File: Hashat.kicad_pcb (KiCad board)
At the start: 2 copper layers, 65 x 56.5 mm, 101 parts, among them IC1 BM1397_mode1, J1 Raspberry_Pi_2_3, J3 Conn_01x05, J4 Conn_01x04, Q1 CSD17311Q5, Q2 CSD17311Q5, U1 25MHz, U10 DS4432U+, U3 SN74AXC1T45DBVR, U5 MCP1824T-1802E, U6 MCP1824T-0802E, U7 EMC2101, U9 TPS40305

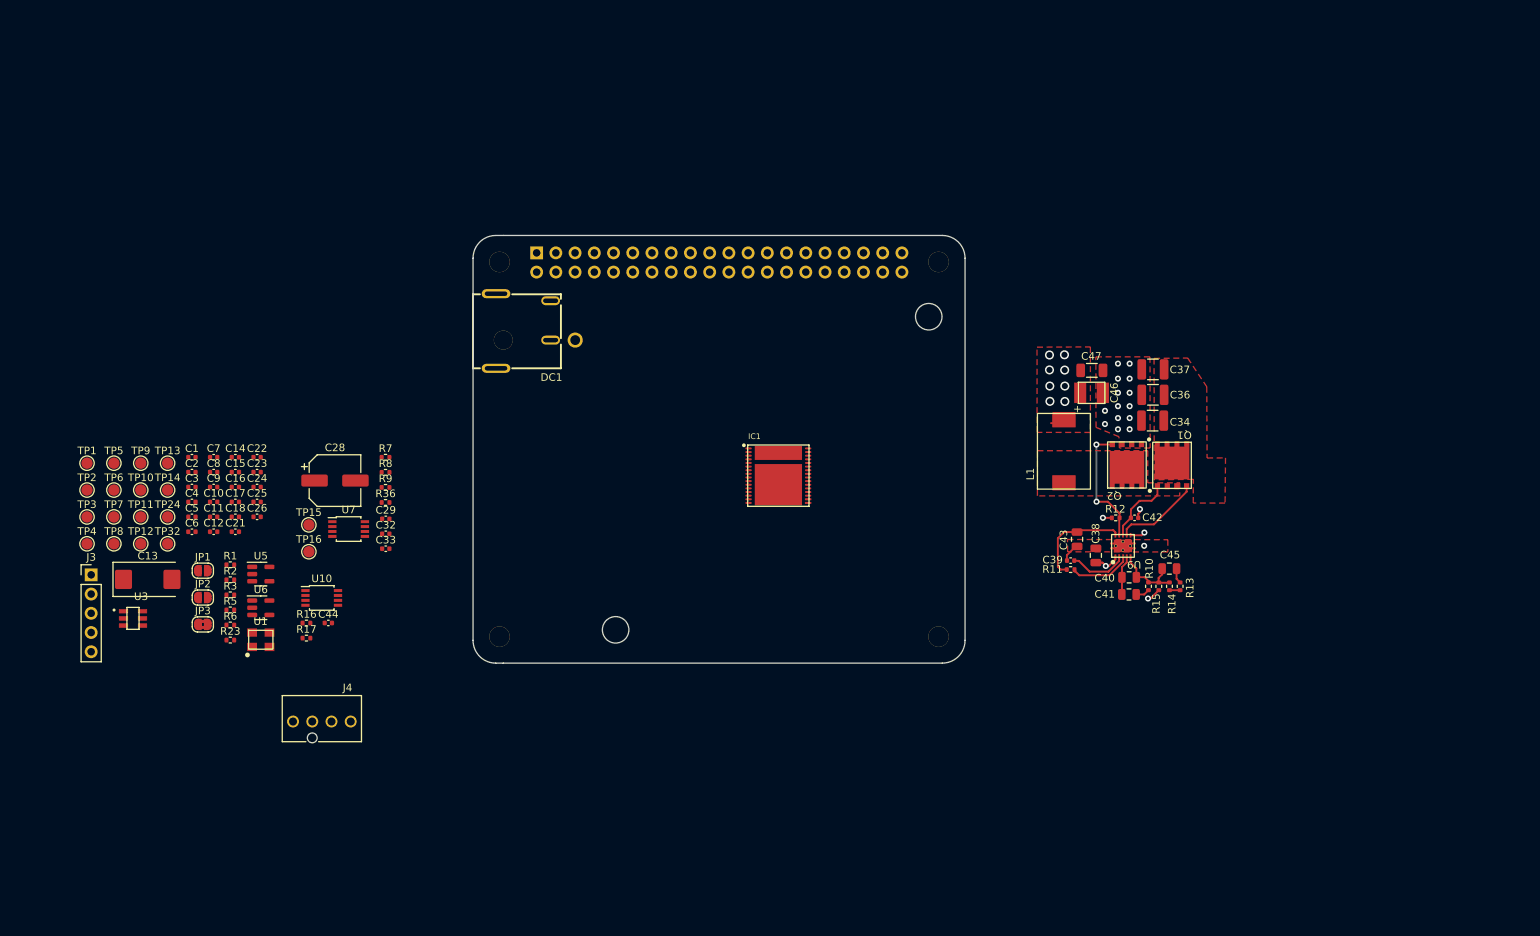
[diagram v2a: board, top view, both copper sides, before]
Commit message: matched up layout ref with schematic
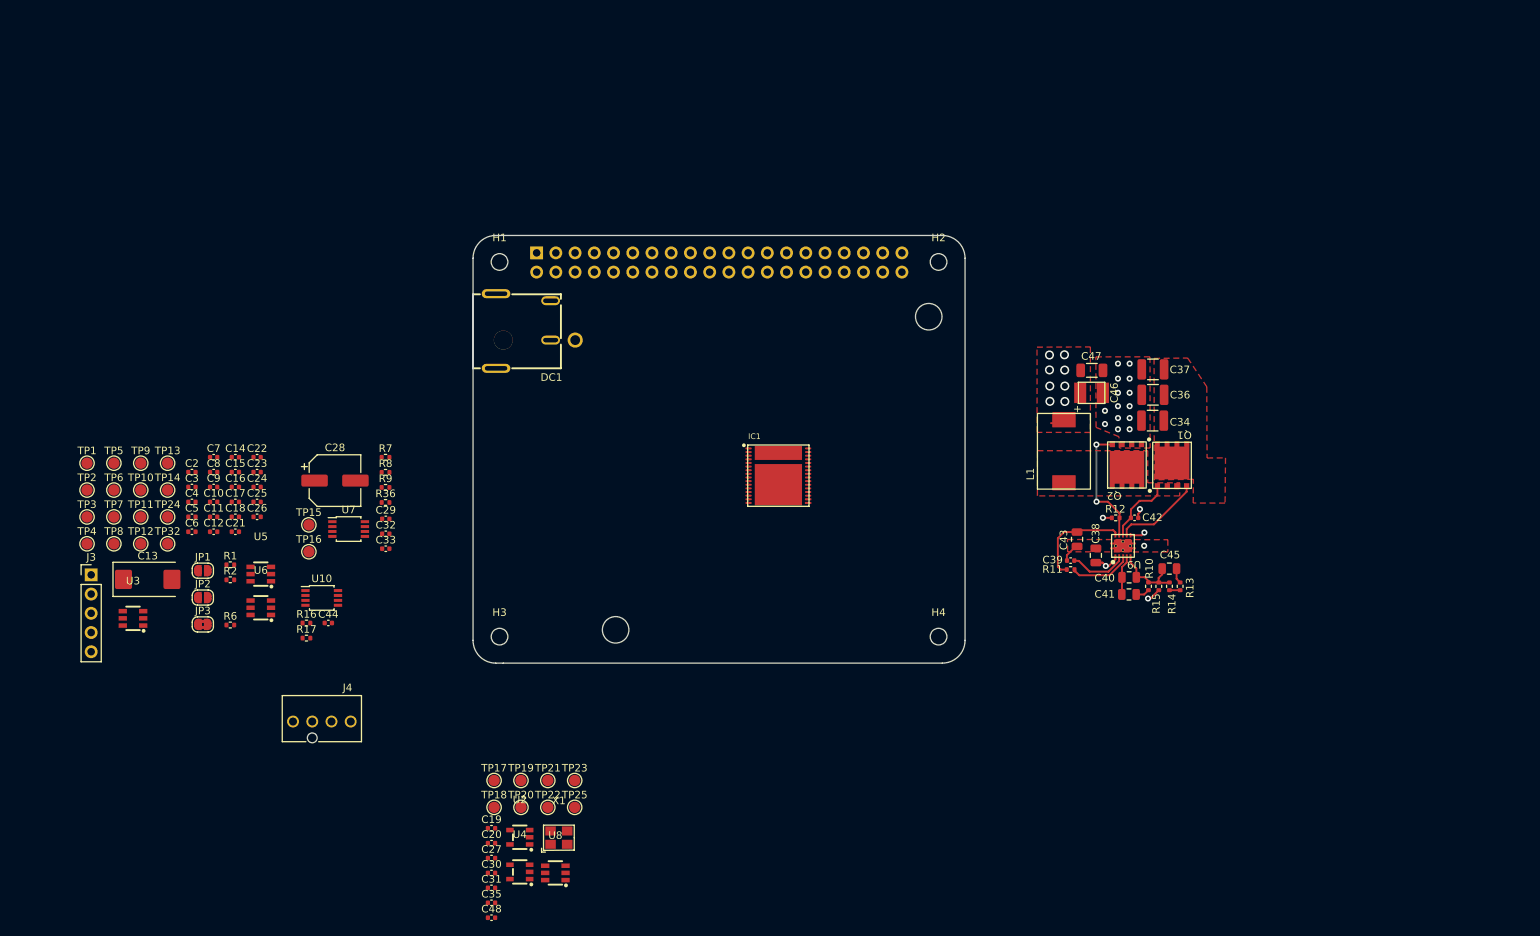
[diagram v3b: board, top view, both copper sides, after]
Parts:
- removed C1: 311-3342-1-ND, Capacitor_SMD:C_0402_1005Metric
- removed R23, R3, R5: 0, Resistor_SMD:R_0402_1005Metric
- removed U1: 25MHz, bitaxe:O 25,0-JO32-B-1V3-1-T1-LF
- added C19: 1uF, Capacitor_SMD:C_0402_1005Metric, F.Cu at (79.4, 133.8)
- added C20: 2.2uF, Capacitor_SMD:C_0402_1005Metric, F.Cu at (79.4, 135.8)
- added C27: 311-3342-1-ND, Capacitor_SMD:C_0402_1005Metric, F.Cu at (79.4, 137.8)
- added C30: 311-3342-1-ND, Capacitor_SMD:C_0402_1005Metric, F.Cu at (79.4, 139.7)
- added C31: 311-3342-1-ND, Capacitor_SMD:C_0402_1005Metric, F.Cu at (79.4, 141.7)
- added C35: 311-3342-1-ND, Capacitor_SMD:C_0402_1005Metric, F.Cu at (79.4, 143.7)
- added C48: 311-3342-1-ND, Capacitor_SMD:C_0402_1005Metric, F.Cu at (79.4, 145.6)
- added TP17: TestPoint, TestPoint:TestPoint_Pad_D1.5mm, F.Cu at (79.8, 127.5)
- added TP18: TestPoint, TestPoint:TestPoint_Pad_D1.5mm, F.Cu at (79.8, 131.1)
- added TP19: TestPoint, TestPoint:TestPoint_Pad_D1.5mm, F.Cu at (83.3, 127.5)
- added TP20: TestPoint, TestPoint:TestPoint_Pad_D1.5mm, F.Cu at (83.3, 131.1)
- added TP21: TestPoint, TestPoint:TestPoint_Pad_D1.5mm, F.Cu at (86.9, 127.5)
- added TP22: TestPoint, TestPoint:TestPoint_Pad_D1.5mm, F.Cu at (86.9, 131.1)
- added TP23: TestPoint, TestPoint:TestPoint_Pad_D1.5mm, F.Cu at (90.4, 127.5)
- added TP25: TestPoint, TestPoint:TestPoint_Pad_D1.5mm, F.Cu at (90.4, 131.1)
- added U2: LN1134A182MR-G, lcsc:SOT-23-5_L3.0-W1.7-P0.95-LS2.8-BR, F.Cu at (83.2, 135.0)
- added U4: SGM2036-ADJYN5G/TR, lcsc:SOT-23-5_L3.0-W1.7-P0.95-LS2.8-BR, F.Cu at (83.2, 139.6)
- added U8: SN74LVC1T45DBVR, lcsc:SOT-23-6_L2.9-W1.6-P0.95-LS2.8-BR, F.Cu at (87.9, 139.7)
- added X1: OT322525MJBA4SL, lcsc:OSC-SMD_4P-L3.2-W2.5-BL, F.Cu at (88.3, 135.1)
- C22: value 311-3342-1-ND -> 1uF
- C25: value 1uF -> 311-3342-1-ND
- H1, H2, H3, H4: renamed from REF**; value MountingHole_2.7mm_M2.5 -> AlignmentHole; footprint MountingHole:MountingHole_2.7mm_M2.5 -> MountingHole:MountingHole_2.2mm_M2
- U3: value SN74AXC1T45DBVR -> SN74LVC1T45DBVR; footprint bitaxe:SN74AXC1T45 -> lcsc:SOT-23-6_L2.9-W1.6-P0.95-LS2.8-BR
- U5: value MCP1824T-1802E -> SN74LVC1T45DBVR; footprint Package_TO_SOT_SMD:SOT-23-5 -> lcsc:SOT-23-6_L2.9-W1.6-P0.95-LS2.8-BR
- U6: value MCP1824T-0802E -> SN74LVC1T45DBVR; footprint Package_TO_SOT_SMD:SOT-23-5 -> lcsc:SOT-23-6_L2.9-W1.6-P0.95-LS2.8-BR
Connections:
- C23 pad 1: /5V -> /BM1397/1V8
- C24 pad 1: /BM1397/1V8 -> /BM1397/0V8
- C25 pad 1: /BM1397/0V8 -> /BM1397/3V3
- IC1 pad 10: Net-(IC1-RO) -> /BM1397/RO
- IC1 pad 11: Net-(IC1-CI) -> /BM1397/CI
- IC1 pad 8: /BM1397/BM_BI -> /BM1397/BI
- TP13 pad 1: /BM1397/1V8 -> /BM1397/0V8
- TP14 pad 1: /BM1397/0V8 -> /BM1397/CI
- TP24 pad 1: /BM1397/BM_BI -> /BM1397/BI
- U3 pad 3: Net-(U3-A) -> /BM1397/RO
- U3 pad 4: /BM1397/CLKI -> /BM1397/BM_RO
- U3 pad 5: GND -> /BM1397/1V8
- U5 pad 1: /5V -> /BM1397/1V8
- U5 pad 3: /5V -> /BM1397/CI
- U5 pad 4: unconnected-(U5-PG-Pad4) -> /BM1397/BM_CI
- U5 pad 5: /BM1397/1V8 -> GND
- U6 pad 1: /5V -> /BM1397/1V8
- U6 pad 3: /5V -> /BM1397/BI
- U6 pad 4: unconnected-(U6-PG-Pad4) -> /BM1397/BM_BI
- U6 pad 5: /BM1397/0V8 -> GND

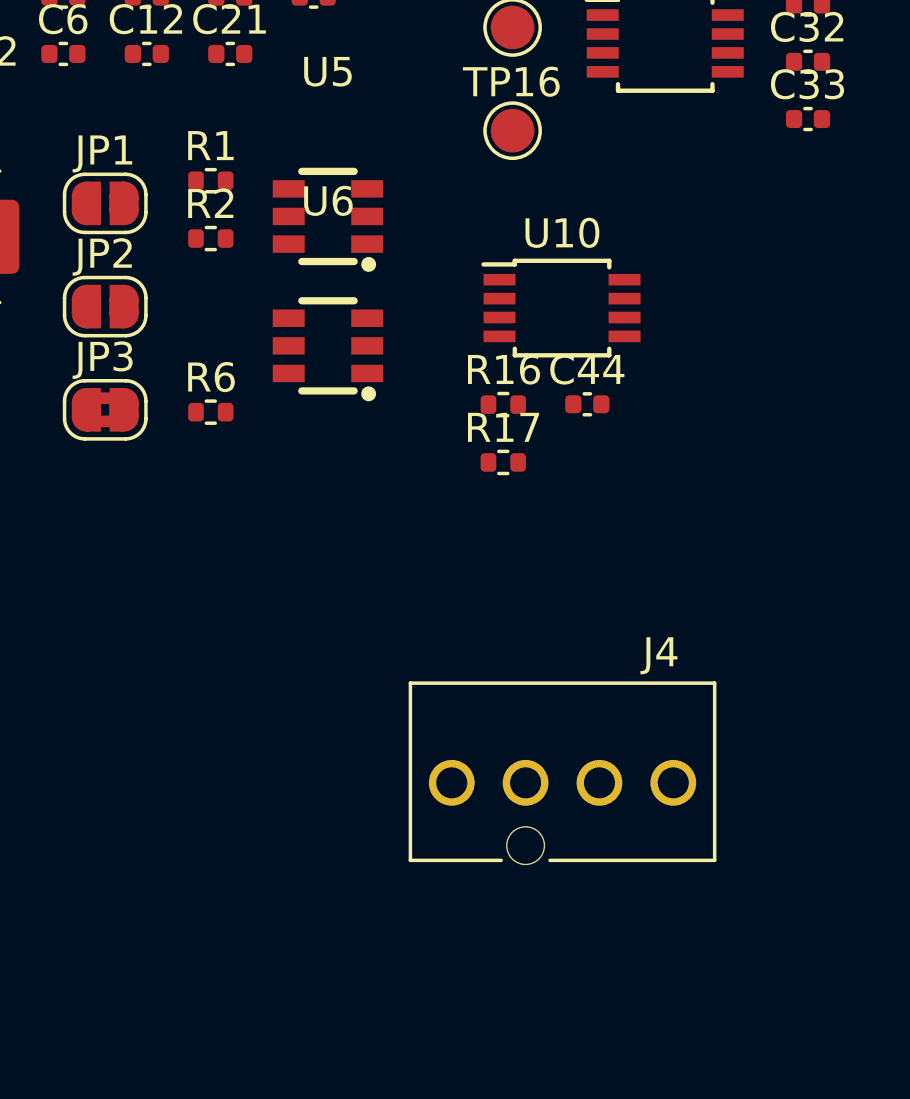
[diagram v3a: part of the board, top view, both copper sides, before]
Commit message: cleanup. added LCSC fan connector
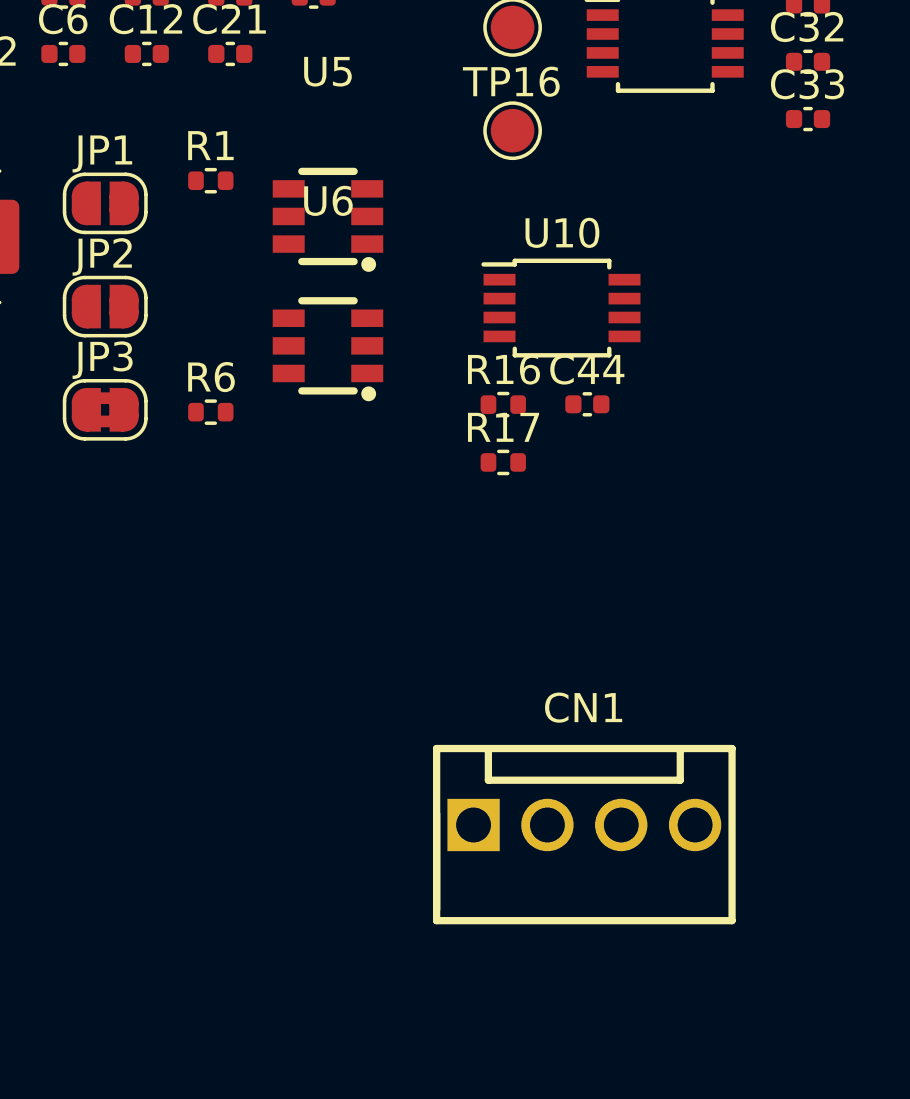
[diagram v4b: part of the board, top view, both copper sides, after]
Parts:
- removed J4: Conn_01x04, bitaxe:470531000
- removed R2: 0, Resistor_SMD:R_0402_1005Metric
- added CN1: HF1004E, lcsc:CONN-TH_4P-P2.54_A2510S-4P, F.Cu at (57.8, 121.2)
- R36: value 10k -> 5.6k
- U7: value EMC2101 -> EMC2101-R
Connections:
- IC1 pad 12: /BM1397/BM_CLKI -> Net-(IC1-CLKI)
- TP1 pad 1: Net-(X1-OUT) -> Net-(IC1-CLKI)
- X1 pad 3: Net-(X1-OUT) -> Net-(IC1-CLKI)

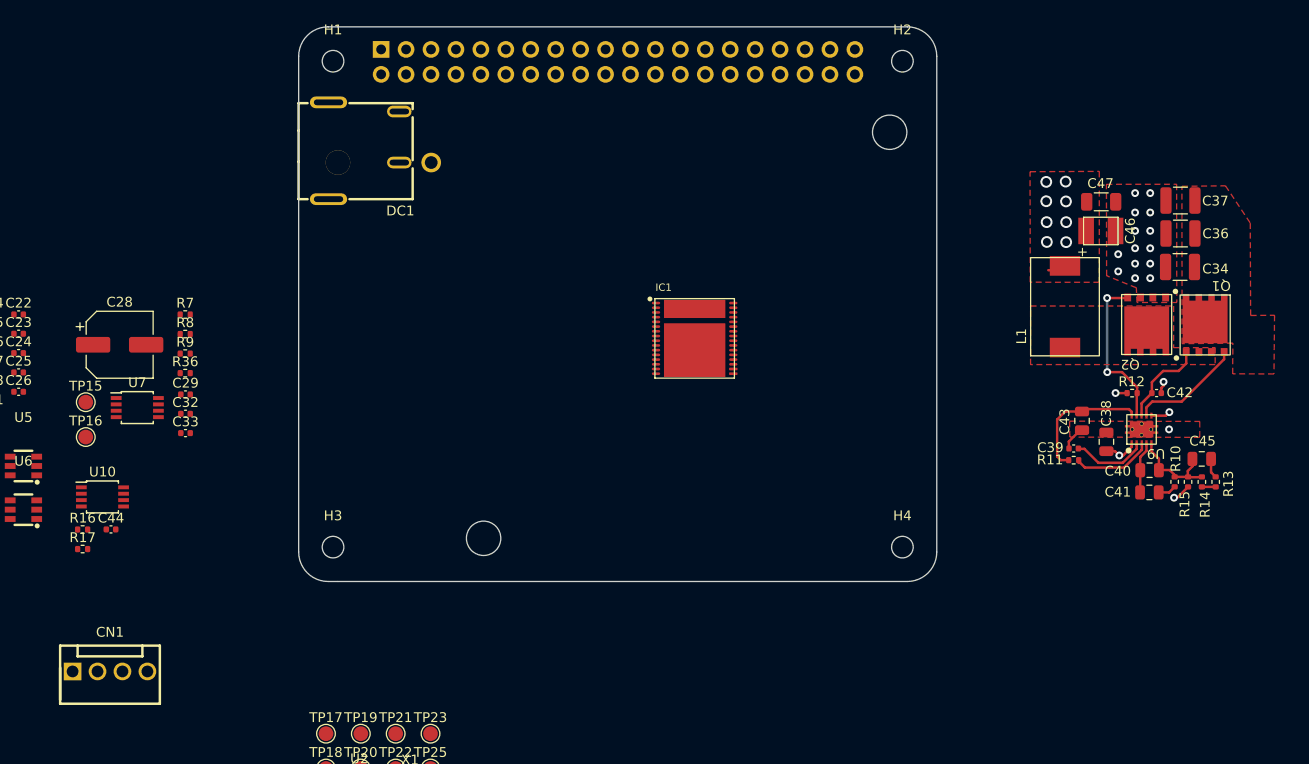
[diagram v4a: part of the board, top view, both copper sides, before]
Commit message: started on new LM5085 based buck design
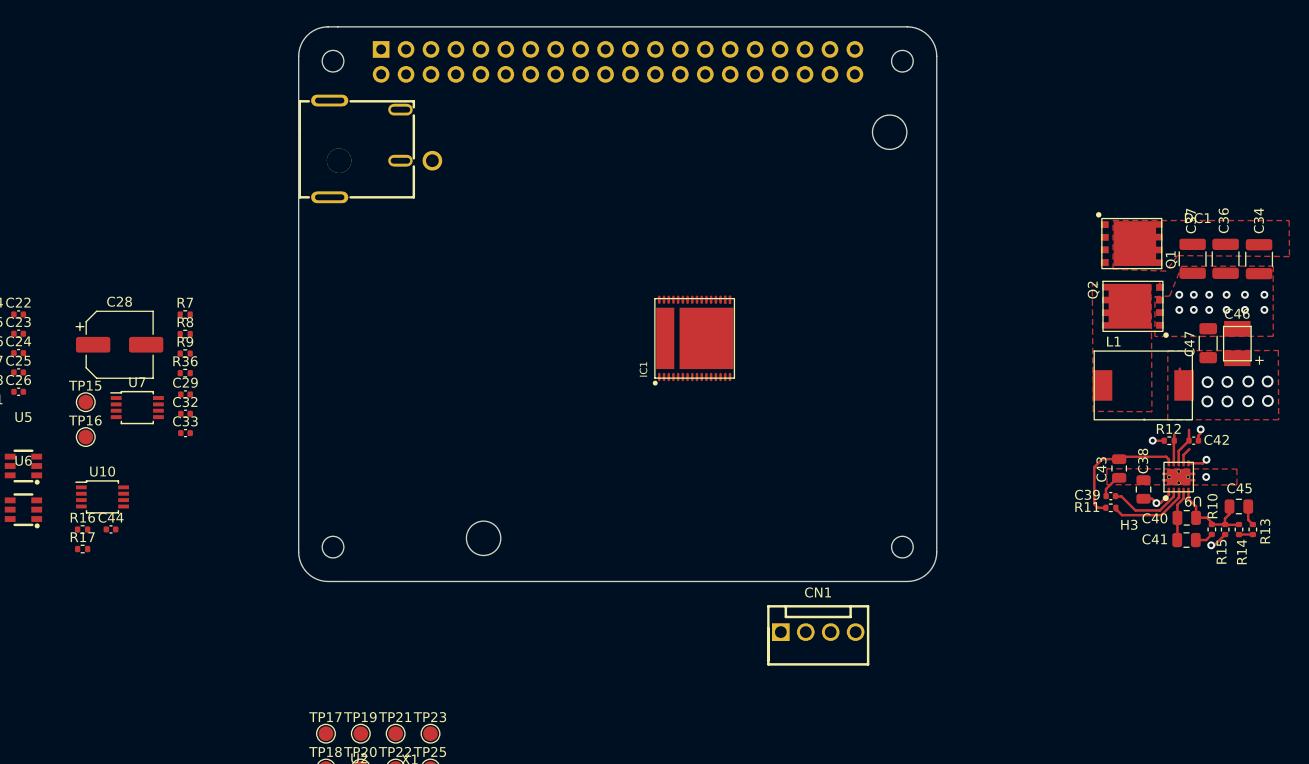
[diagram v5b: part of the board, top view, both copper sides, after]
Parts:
- moved CN1 72.3 mm to (129.9, 117.2)
- moved C47 18.1 mm to (169.7, 87.7), turned to 90 degrees
- moved C46 18.0 mm to (172.6, 87.8), turned to 90 degrees
- moved L1 11.3 mm to (163.0, 92.0), turned to 0 degrees
- moved Q1 11.2 mm to (161.9, 77.6), turned to 180 degrees
- moved C34 8.09 mm to (174.8, 79.2), turned to -90 degrees
- moved C40 6.15 mm to (167.5, 105.5)
- moved U9 6.15 mm to (166.6, 101.4)
- moved R10 6.15 mm to (170.0, 106.7)
- moved R12 6.15 mm to (165.7, 97.7)
- moved C38 6.15 mm to (163.1, 102.6)
- moved C39 6.15 mm to (159.7, 103.3)
- moved C41 6.15 mm to (167.4, 107.8)
- moved C42 6.15 mm to (168.2, 97.7)
- moved C43 6.15 mm to (160.6, 100.5)
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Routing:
- net Net-(Q2-G): track 16.3 -> 3.33 mm, vias 2 -> 0
- net Net-(Q1-G): track 11.5 -> 1.69 mm
- net /Power/SW: track 9.30 -> 3.85 mm
- net GND: vias 17 -> 15
